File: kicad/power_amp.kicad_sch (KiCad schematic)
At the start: 15 parts

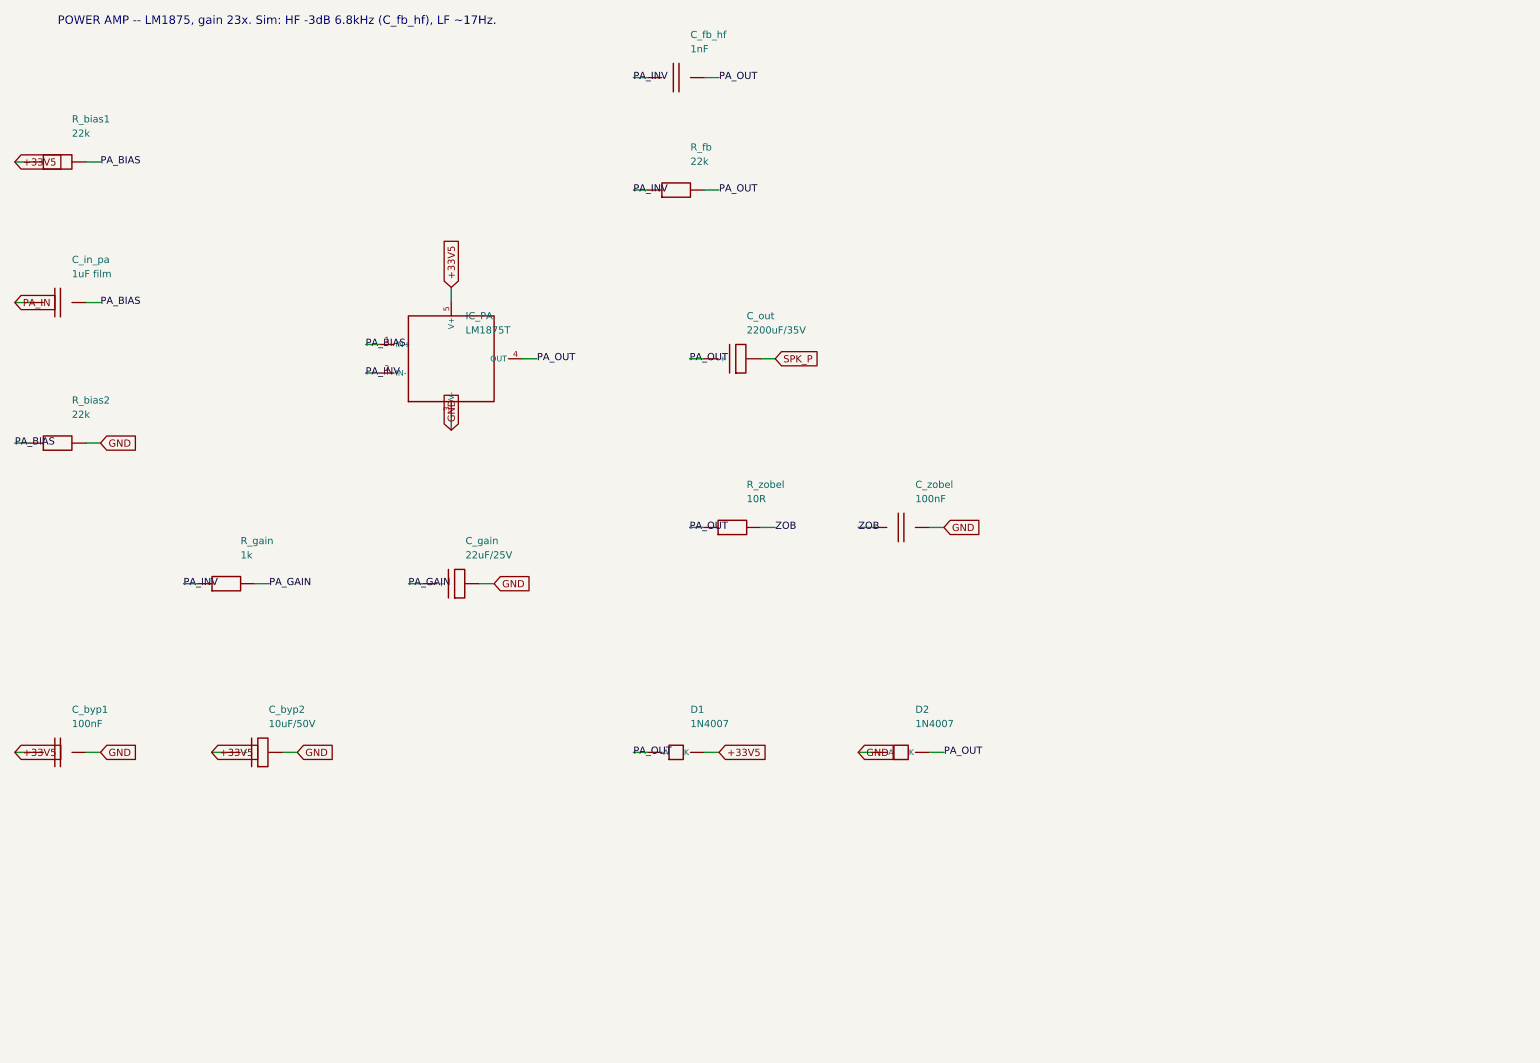
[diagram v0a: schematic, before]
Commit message: Schematic passes KiCad 8 ERC (0 violations); add op-amp mid-rail bias
Installed KiCad 8.0.9 and ran a real Electrical Rules Check on the generated
hierarchy. Drove it to 0 violations:
- snapped every pin/wire endpoint to the 1.27 mm connection grid (was 338
  endpoint_off_grid violations)
- gave the footswitch lines FS_REV/FS_TREM/FS_MRB a real second endpoint via
  100k control pulldowns on the reverb/tremolo/mrb sheets (was 3 dangling labels)

Also made the single-supply TL072 stages electrically real: added a mid-rail
VBIAS network (R_vb1/R_vb2 + C_vb on the Power Supply sheet) and referenced the
reverb driver and tremolo LFO inputs/gain-returns to VBIAS instead of GND
(design addition, flagged in the sheet notes).

Result: kicad-cli 8.0.9 sch erc -> 0 violations; netlist 102 components, 58
nets, 0 unconnected pins; VBIAS spans 10 nodes. Updated SCHEMATIC-BUILD.md,
kicad/README.md, CHANGELOG.md.

https://claude.ai/code/session_01PkrfUi9tvZfLvudJ7h23qD
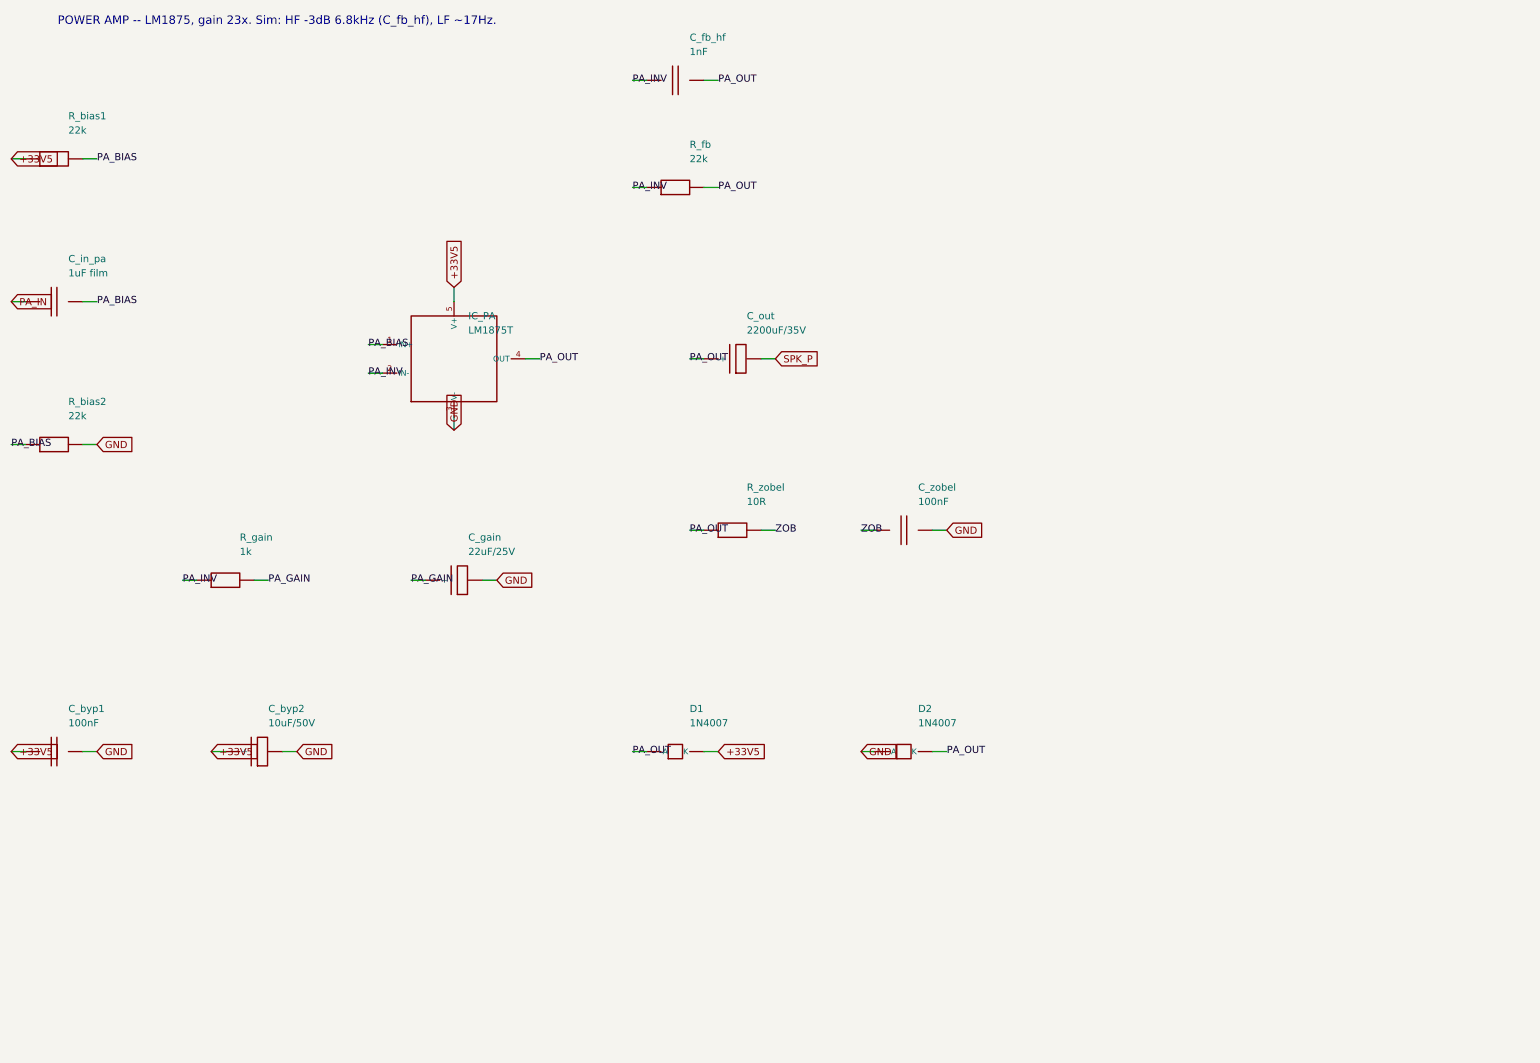
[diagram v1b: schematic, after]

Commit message: Generate auto-placed PCB (102 footprints, GND pour, board outline)
Build cambridge_reverb.kicad_pcb from the schematic via kicad/gen/gen_pcb.py
(KiCad 8 pcbnew API): assign a THT footprint to every component (standard libs
for generics + the project footprints for VTL5C1 and the 1H toroid), place all
102 footprints (off-board connectors on a bottom wiring-edge strip, toroid in a
reserved spot), assign all 58 nets to pads, draw a 190x115 mm Edge.Cuts outline,
and pour a bottom-layer GND plane. Footprint assignments also carry into the
schematic symbols.

The board opens in KiCad and the ratsnest matches the ERC-clean schematic. It is
placed but NOT routed: kicad-cli pcb drc is dominated by 130 unconnected
(unrouted signal nets; GND is poured) plus cosmetic silk/courtyard overlaps from
dense auto-placement at chassis size -- documented in kicad/PCB-NOTES.md with the
remaining hand-work (placement into floor-plan zones, routing, DRC-to-zero,
Gerbers). Net classes (Default/Power/HighCurrent) carry over for routing.

Also: schematic resistor footprint switched to the compact vertical variant;
gitignore DRC/ERC .rpt reports.

https://claude.ai/code/session_01PkrfUi9tvZfLvudJ7h23qD
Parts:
- C_byp1, C_fb_hf, C_in_pa, C_zobel: footprint (none) -> Capacitor_THT:C_Disc_D7.5mm_W2.5mm_P5.00mm
- C_byp2, C_gain, C_out: footprint (none) -> Capacitor_THT:CP_Radial_D8.0mm_P3.50mm
- D1, D2: footprint (none) -> Diode_THT:D_DO-41_SOD81_P10.16mm_Horizontal
- IC_PA: footprint (none) -> Package_TO_SOT_THT:TO-220-5_Vertical
- R_bias1, R_bias2, R_fb, R_gain, R_zobel: footprint (none) -> Resistor_THT:R_Axial_DIN0207_L6.3mm_D2.5mm_P5.08mm_Vertical

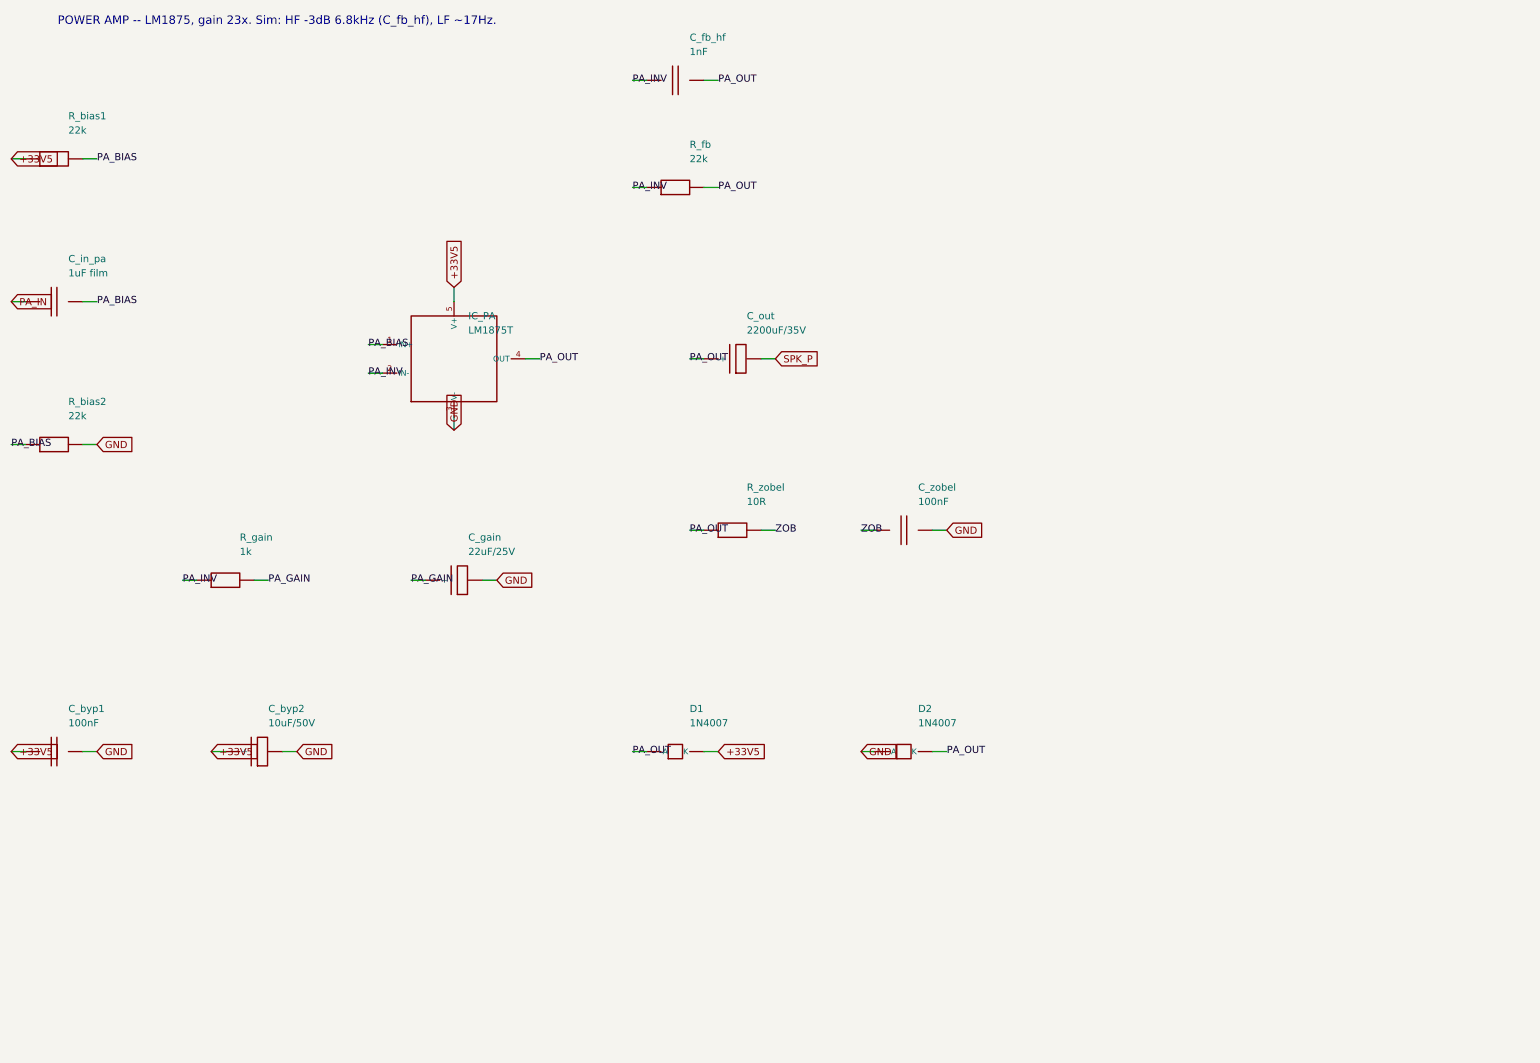
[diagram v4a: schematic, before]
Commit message: Audit pass: center schematic pages, PCB layout audit, SPICE audit
Schematic: gen_kicad.py now defers draw-op emission, computes each sheet's
content bounding box, and translates it to the page center (grid-snapped so pins
stay on the 1.27mm grid). All 8 sheets are centered on the page instead of
crammed top-left; ERC still 0 violations.

PCB: full category-by-category audit in kicad/PCB-AUDIT.md (footprints,
placement, net classes, copper/GND, routing) with prioritized fixes. Applied:
- the 5 reused/off-board pots were modeled with a 16mm panel-pot footprint; they
  are panel-mounted (wired off-board), so they're now 3-pad wiring connectors --
  more correct and a big silk-overlap source removed (packing 51%->48%)
- centered the component grid
Documented findings: LM1875 TO-220-5 annular is 0.0875mm (1.275mm pad on 1.1mm
drill) vs the 0.15mm rule; KBP410G bridge uses a placeholder header footprint;
silk/courtyard overlaps are a density symptom (the 82% packing on the 155x90
safe-bet). Non-routing DRC errors: 9; demo board still 0.

SPICE: audited every netlist/model (spice/README.md). All five run under
ngspice-42 (exit 0) and match the documented numbers; no correctness issues.

https://claude.ai/code/session_01PkrfUi9tvZfLvudJ7h23qD
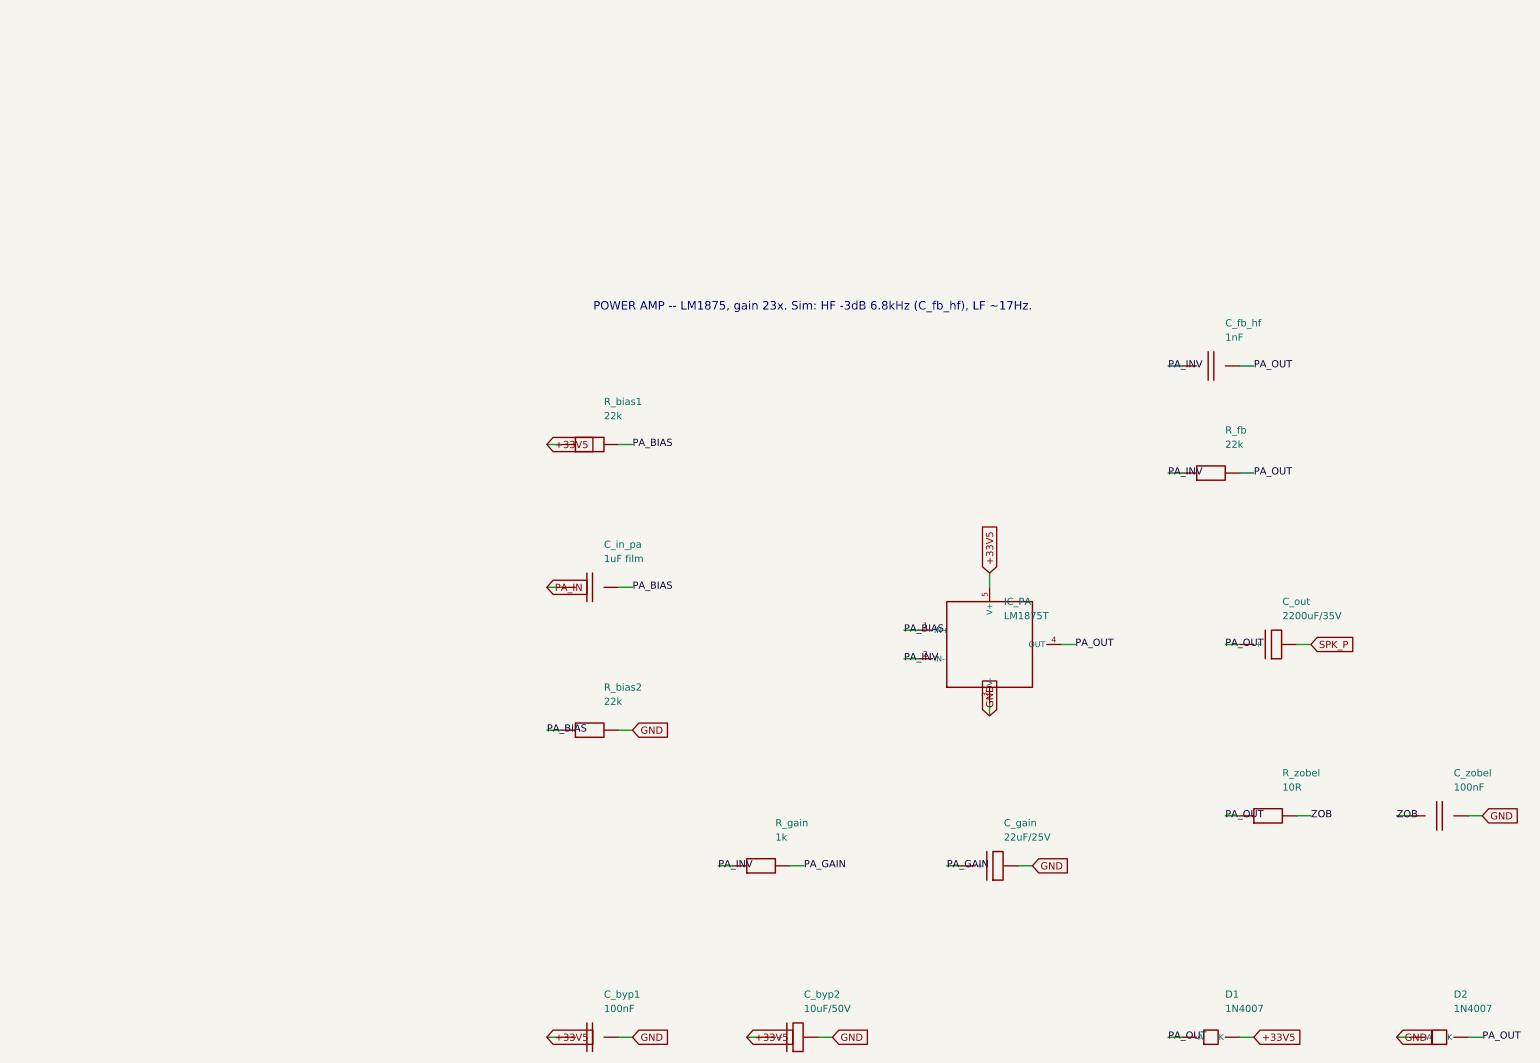
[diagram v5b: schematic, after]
